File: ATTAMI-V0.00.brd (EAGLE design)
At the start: 22.8 x 22.9 mm, 26 parts, among them U1 MIC5225, U2 ATTINY85-20SU, U3 1117

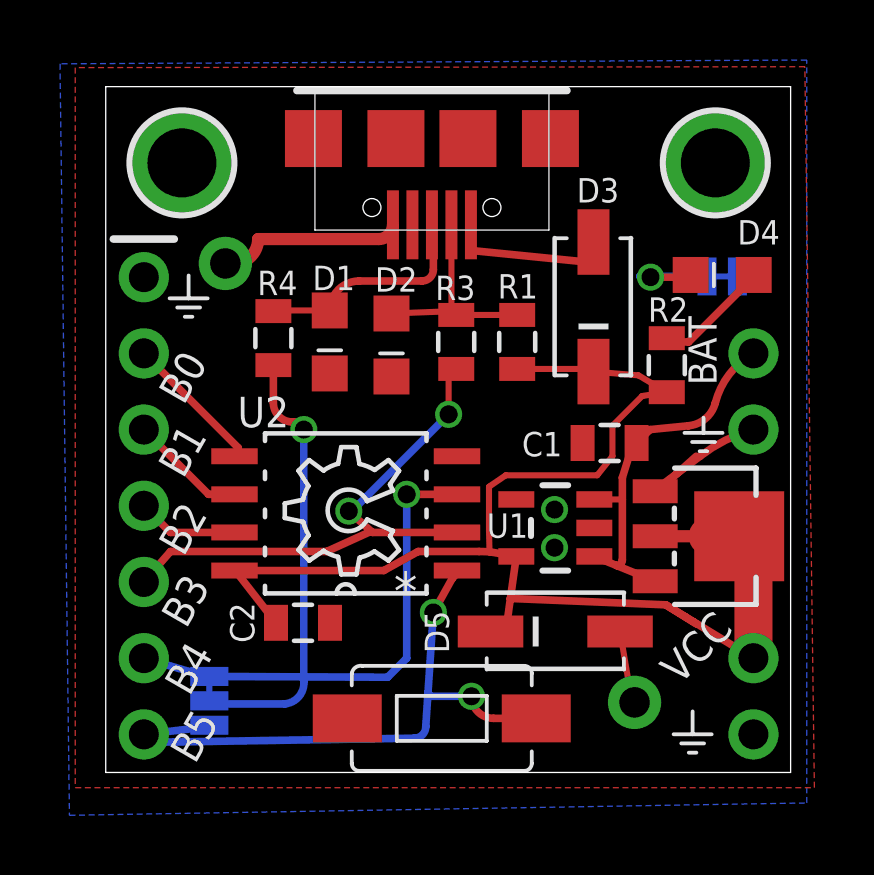
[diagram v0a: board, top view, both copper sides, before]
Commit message: fixed some airwires in the board, and new panelize
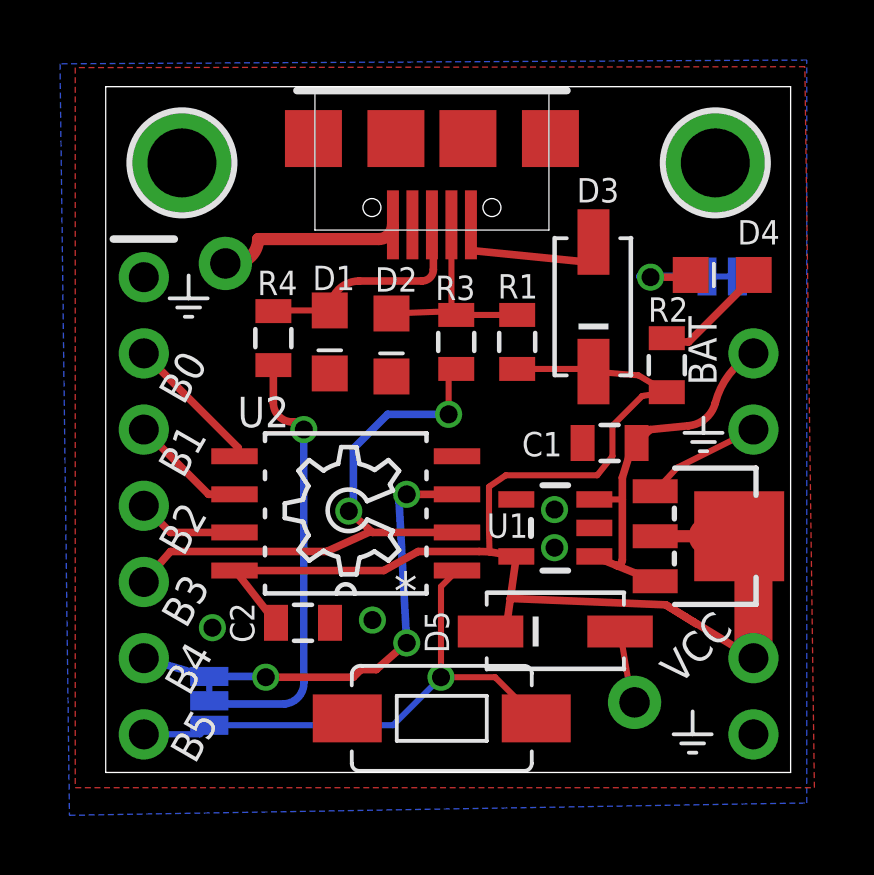
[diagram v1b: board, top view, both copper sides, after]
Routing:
- net PB5: track 21.3 -> 18.2 mm, vias 2 -> 1
- net GND: track 12.0 -> 10.0 mm, vias 2 -> 4
- net PB3: track 21.2 -> 22.4 mm
- net PB4: track 16.3 -> 16.1 mm, vias 1 -> 3
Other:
- board text added: "V 1.1"
- board text removed: "V 0.00"

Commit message: a versin without the fancy LDO and SOT0232 for the X1117
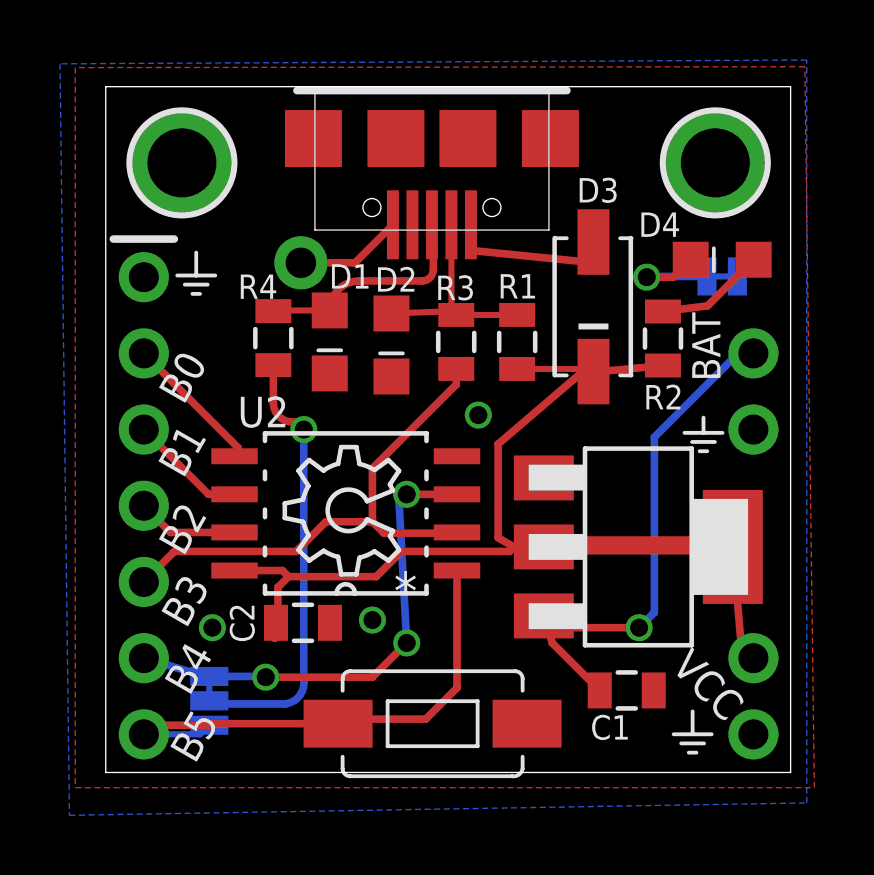
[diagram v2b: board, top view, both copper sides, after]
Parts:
- removed COIN_CELL_(+): (no value), ATtami:1X01-CLEANBIG
- removed D5: Schottky, ATtami:SOD-323
- removed U1: MIC5225, ATtami:SOT23-5
- U3: device ATtami:SOT89 -> ATtami:SOT-223
- moved C1 8.27 mm to (17.4, 2.73), turned to 0 degrees
- moved COIN_CELL_(-) 2.52 mm to (6.51, 17.0), turned to 6 degrees
- moved U3 2.34 mm to (17.8, 7.52)
- moved R2 0.90 mm to (18.6, 14.5)
- moved D4 0.51 mm to (20.6, 17.1)
- moved S1 0.35 mm to (10.9, 1.63), turned to 0 degrees
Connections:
- removed net N$4: COIN_CELL_(+).1, D5.AQ
- net GND: now also U3.1; no longer U1.2, U3.GND
- net VCC: now also U3.2, U3.4; no longer D5.CQ, U1.5, U3.VOUT@1, U3.VOUT@2
- net V_BAT: now also U3.3; no longer U1.1, U1.3, U3.VIN
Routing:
- net VCC: track 48.1 -> 38.0 mm
- net GND: track 10.0 -> 3.59 mm, vias 4 -> 3
- net PB3: track 22.4 -> 17.7 mm, vias 2 -> 0
- net V_BAT: track 13.0 -> 17.5 mm, vias 0 -> 1
- net N$4: track 2.44 -> 0.00 mm
- net N$11: track 4.38 -> 3.67 mm
- net PB5: track 18.2 -> 17.9 mm, vias 1 -> 0

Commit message: moved power led jumper to top layer
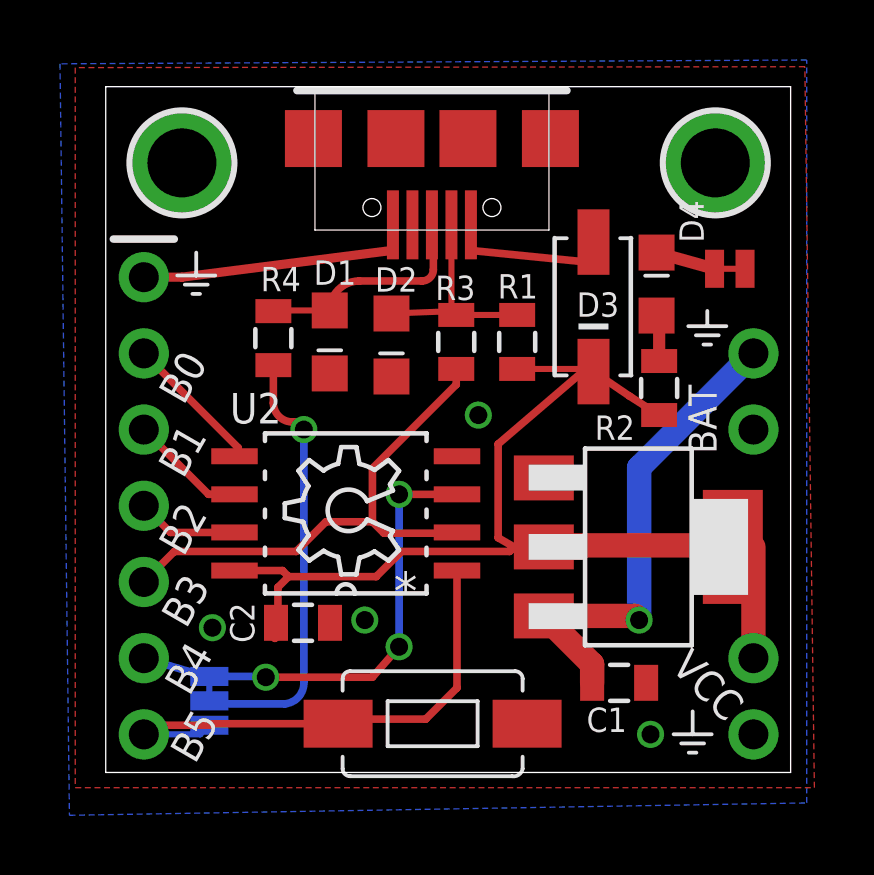
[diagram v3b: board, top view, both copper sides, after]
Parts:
- removed COIN_CELL_(-): (no value), ATtami:1X01-CLEANBIG
- moved D4 2.33 mm to (18.4, 16.3), turned to 180 degrees
- moved R2 1.66 mm to (18.4, 12.8)
- moved SJ1 0.36 mm to (20.8, 16.8), flipped to the top, turned to 180 degrees
- moved C1 0.36 mm to (17.1, 2.99)
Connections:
- net GND: no longer COIN_CELL_(-).1
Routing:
- net GND: track 3.59 -> 9.22 mm, vias 3 -> 4
- net N$11: track 3.67 -> 1.60 mm
- net N$13: track 3.72 -> 2.01 mm, vias 1 -> 0
- net V_BAT: track 17.5 -> 16.6 mm
- net VCC: track 38.0 -> 38.8 mm
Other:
- board text added: "V-BAT"
- board text removed: "+"

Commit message: gerbering to fab
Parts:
- removed U3: 1117, ATtami:SOT-223
- added U1: ATTINY85-20SU, ATtami:SOIC127P798X216-8N
- U2: value ATTINY85-20SU -> (none); device ATtami:SOIC127P798X216-8N -> ATtami:SOT-223
- moved U2 9.82 mm to (17.8, 7.52), turned to 270 degrees
- moved D4 1.61 mm to (20.0, 16.4), turned to 90 degrees
- moved SJ1 0.40 mm to (20.9, 16.4), flipped to the bottom
- moved R2 0.38 mm to (18.4, 13.2)
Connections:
- net GND: now also U1.4, U2.1; no longer U2.4, U3.1
- net PB0: now also U1.5; no longer U2.5
- net PB1: now also U1.6; no longer U2.6
- net PB2: now also U1.7; no longer U2.7
- net PB3: now also U1.2; no longer U2.2
- net PB4: now also U1.3; no longer U2.3
- net PB5: now also U1.1; no longer U2.1
- net VCC: now also U1.8, U2.2, U2.4; no longer U2.8, U3.2, U3.4
- net V_BAT: now also U2.3; no longer U3.3
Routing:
- net N$13: track 2.01 -> 3.33 mm, vias 0 -> 1
- net N$11: track 1.60 -> 2.43 mm
